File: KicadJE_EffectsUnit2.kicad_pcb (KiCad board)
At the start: 2 copper layers, 100 x 100 mm, 69 parts, among them J201 In_1, J202 In 2, J203 Out 1, J204 Out 2, J205 Out Final, P201 Doepfer_Power_10pin, SW201 Dist 6, SW202 In or cascade, SW203 In or cascade, SW204 In or cascade, SW205 HI/LO, U201 TL072, U202 TL072

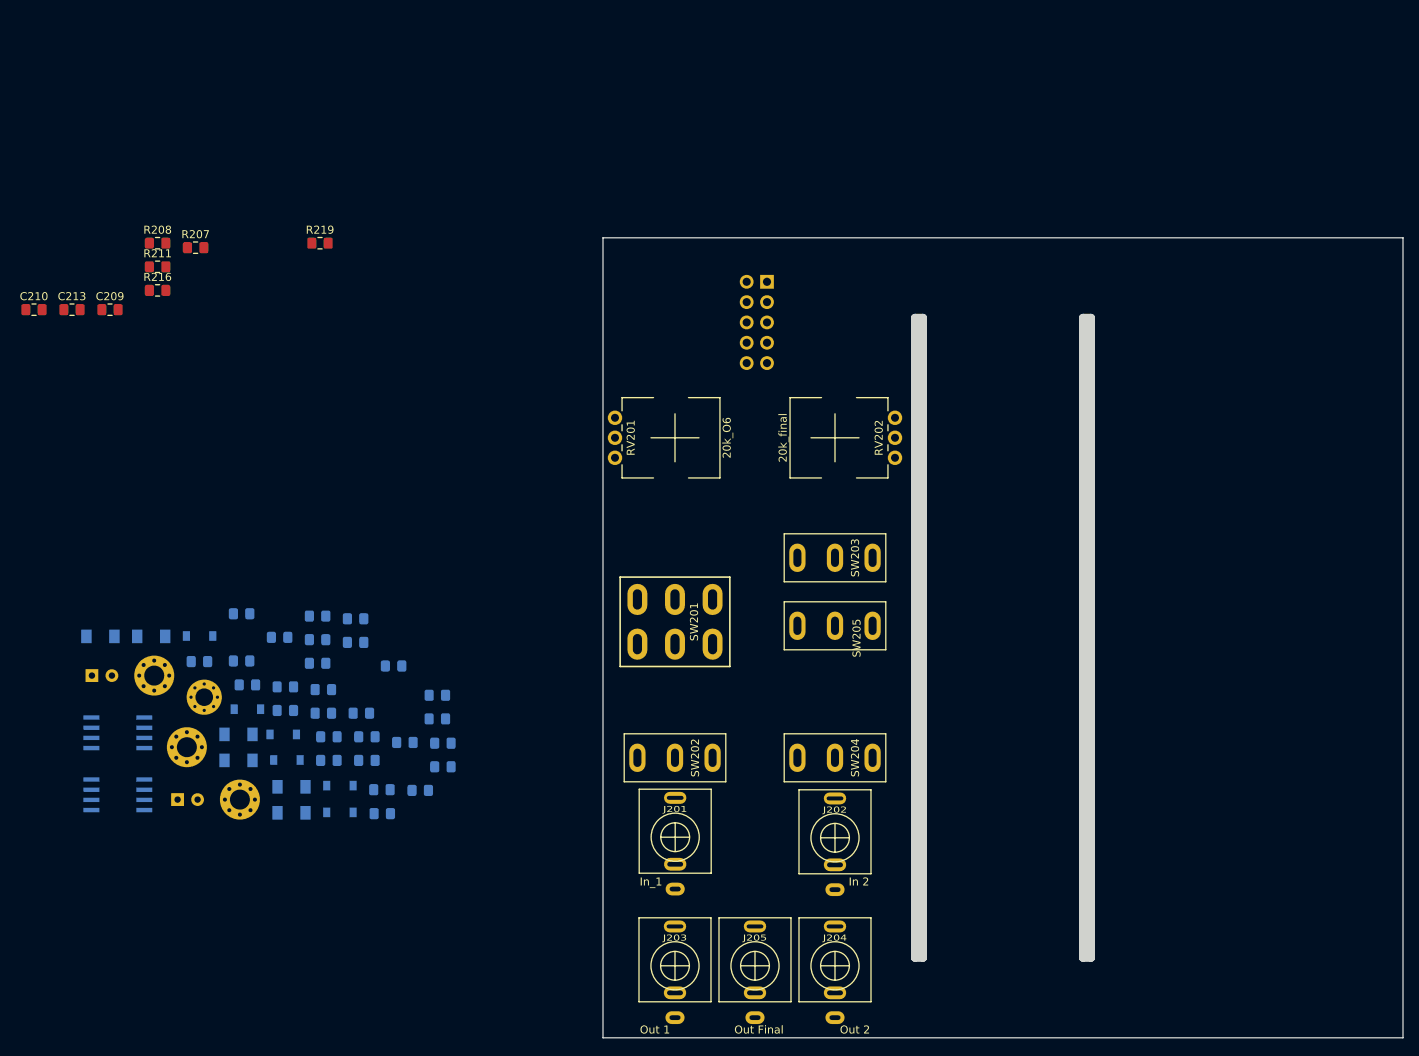
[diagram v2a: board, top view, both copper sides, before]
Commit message: decoupling placed
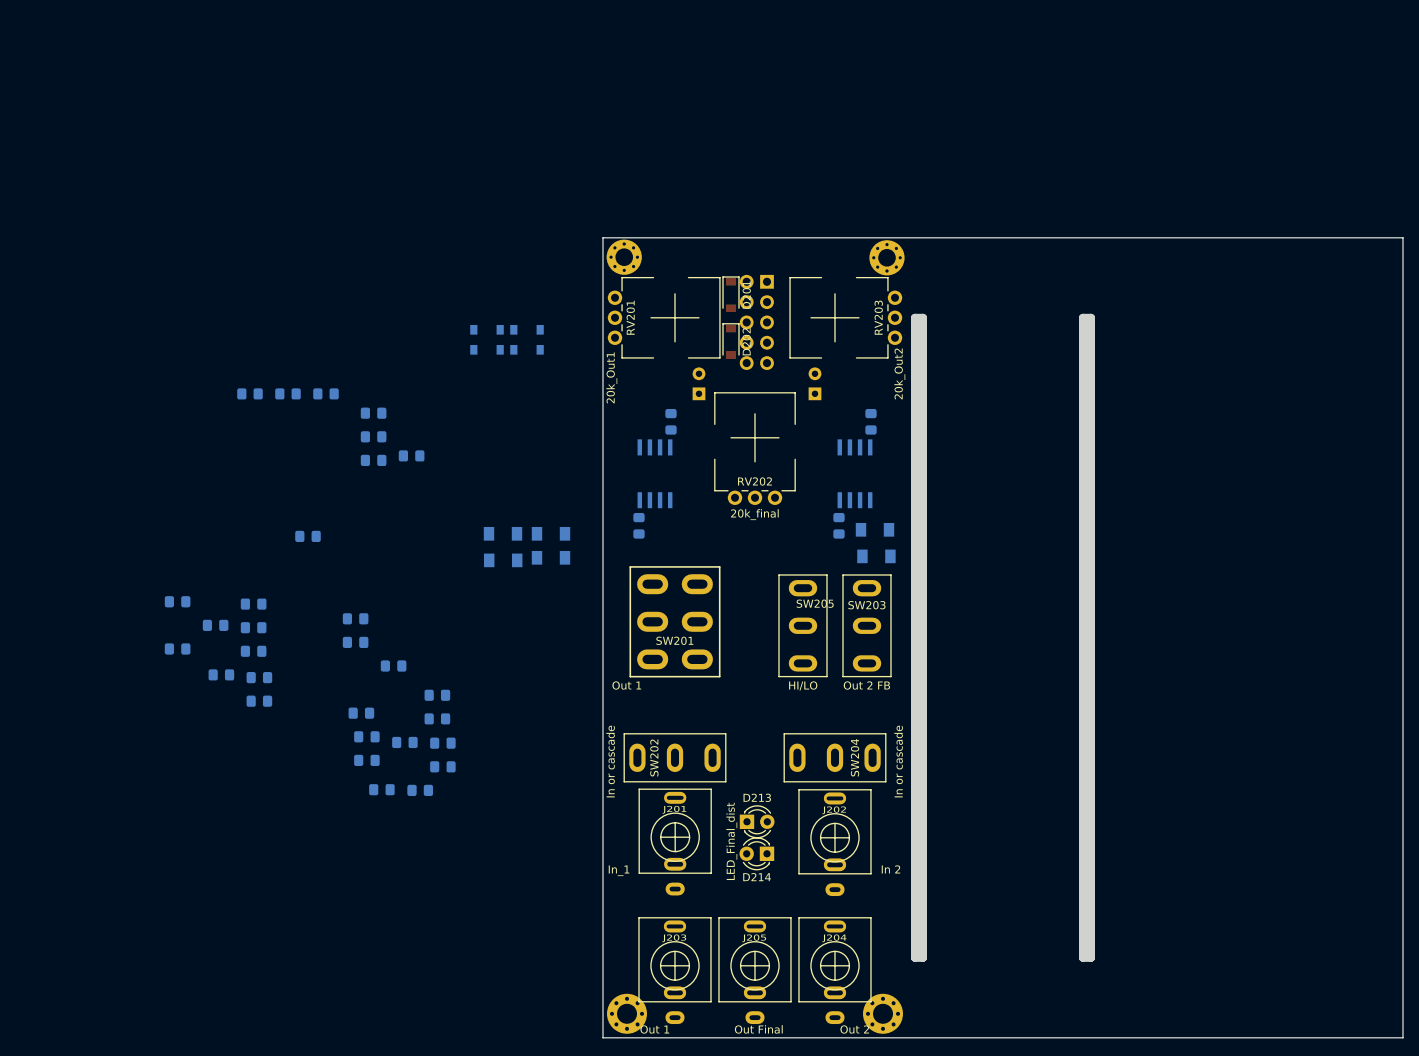
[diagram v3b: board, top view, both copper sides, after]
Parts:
- added RV203: 20k_Out2, Potentiometer_THT:Potentiometer_China_RK09_Single_Vertical_AJ, F.Cu at (86.5, 57.5)
- C209, C210, C213: value 100n -> 220n; moved to B.Cu
- C211: value 100n -> 220n
- D201, D202: moved to F.Cu
- D213: value LED_11dist -> LED_Final_dist; footprint LED_SMD:LED_0805_2012Metric_Pad1.15x1.40mm_HandSolder -> LED_THT:LED_D3.0mm; moved to F.Cu
- D214: value LED_11dist -> LED_Final_dist; footprint Diode_SMD:D_0805_2012Metric_Pad1.15x1.40mm_HandSolder -> LED_THT:LED_D3.0mm; moved to F.Cu
- H203: footprint MountingHole:MountingHole_2.5mm_Pad_Via -> MountingHole:MountingHole_2.2mm_M2_Pad_Via
- R206, R213: value 10k -> 4k7
- R207, R208, R211, R216, R219: moved to B.Cu
- RV201: value 20k_O6 -> 20k_Out1
- SW201: value Dist 6 -> Out 1
- SW203: value In or cascade -> Out 2 FB
- moved H203 105.4 mm to (85.5, 52.5)
- moved U202 100.5 mm to (81.5, 79.5), turned to 90 degrees
- moved D212 97.5 mm to (84.2, 89.8)
- moved C205 94.5 mm to (76.5, 69.5), turned to 90 degrees
- moved H202 93.2 mm to (85.0, 147.0)
- moved C203 89.1 mm to (83.5, 73.0), turned to 270 degrees
- moved D211 84.6 mm to (84.0, 86.5), turned to 180 degrees
- moved C201 83.7 mm to (62.0, 69.5), turned to 90 degrees
- moved D201 80.4 mm to (66.0, 57.1), turned to 270 degrees
- moved D202 76.5 mm to (66.0, 63.0), turned to 270 degrees
- moved H204 76.0 mm to (52.7, 52.4)
- moved U201 74.5 mm to (56.5, 79.5), turned to 90 degrees
- moved C207 73.0 mm to (79.5, 86.0), turned to 270 degrees
- moved D213 64.8 mm to (68.0, 123.0)
- moved D204 59.3 mm to (40.5, 64.0)
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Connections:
- C201 pad 1: (no net) -> /KicadJE_EU7_Distort2/-12v
- C201 pad 2: Net-(C201-Pad2) -> GND
- C202 pad 1: Net-(C202-Pad1) -> GND
- C202 pad 2: (no net) -> /KicadJE_EU7_Distort2/-12v
- C203 pad 1: Net-(C203-Pad1) -> GND
- C203 pad 2: (no net) -> /KicadJE_EU7_Distort2/-12v
- C205 pad 1: Net-(C201-Pad2) -> GND
- C205 pad 2: (no net) -> /KicadJE_EU7_Distort2/+12v
- C206 pad 1: (no net) -> /KicadJE_EU7_Distort2/+12v
- C206 pad 2: Net-(C202-Pad1) -> GND
- C207 pad 1: (no net) -> /KicadJE_EU7_Distort2/+12v
- C207 pad 2: Net-(C203-Pad1) -> GND
- C211 pad 2: (no net) -> Net-(C211-Pad2)
- D201 pad 1: (no net) -> /KicadJE_EU7_Distort2/-12v
- D201 pad 2: Net-(D201-Pad2) -> GND
- D202 pad 1: Net-(D201-Pad2) -> GND
- D202 pad 2: (no net) -> /KicadJE_EU7_Distort2/+12v
- D213 pad 2: OutFinal -> Net-(D213-Pad2)
- D214 pad 1: OutFinal -> Net-(D213-Pad2)
- P201 pad 1: +12V -> /KicadJE_EU7_Distort2/-12v
- P201 pad 10: -12V -> /KicadJE_EU7_Distort2/+12v
- P201 pad 2: +12V -> /KicadJE_EU7_Distort2/-12v
- P201 pad 3: Net-(P201-Pad3) -> GND
- P201 pad 4: Net-(P201-Pad3) -> GND
- P201 pad 5: Net-(P201-Pad3) -> GND
- P201 pad 6: Net-(P201-Pad3) -> GND
- P201 pad 7: Net-(P201-Pad3) -> GND
- P201 pad 8: Net-(P201-Pad3) -> GND
- P201 pad 9: -12V -> /KicadJE_EU7_Distort2/+12v
- R208 pad 2: (no net) -> In1
- R213 pad 2: Net-(R212-Pad1) -> Net-(R213-Pad2)
- R220 pad 1: OutFinal -> Net-(D213-Pad2)
- SW201 pad 2: (no net) -> Net-(D203-Pad2)
- SW203 pad 3: (no net) -> Net-(C211-Pad2)
- U201 pad 4: (no net) -> /KicadJE_EU7_Distort2/+12v
- U201 pad 8: (no net) -> /KicadJE_EU7_Distort2/-12v
- U202 pad 4: (no net) -> /KicadJE_EU7_Distort2/+12v
- U202 pad 5: (no net) -> Net-(D213-Pad2)
- U202 pad 6: (no net) -> OutFinal
- U202 pad 7: (no net) -> OutFinal
- U202 pad 8: (no net) -> /KicadJE_EU7_Distort2/-12v

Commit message: Overall placement
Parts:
- moved C211 101.6 mm to (97.0, 68.0)
- moved R214 99.3 mm to (97.0, 71.0)
- moved R213 98.5 mm to (97.0, 65.0)
- moved R222 90.5 mm to (92.5, 68.0)
- moved R201 85.6 mm to (79.0, 125.5), turned to 90 degrees
- moved C213 85.4 mm to (95.0, 83.0), turned to 180 degrees
- moved R211 76.0 mm to (94.5, 95.5)
- moved R216 73.9 mm to (93.3, 88.4)
- moved R217 72.5 mm to (93.0, 112.8)
- moved R212 70.5 mm to (97.5, 114.5), turned to 180 degrees
- moved R218 69.4 mm to (94.5, 108.5)
- moved C212 65.7 mm to (80.0, 87.5), turned to 270 degrees
- moved R215 65.5 mm to (80.0, 83.5), turned to 90 degrees
- moved C210 54.1 mm to (56.1, 89.5), turned to 180 degrees
- moved R202 50.2 mm to (76.0, 125.5), turned to 270 degrees
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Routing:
- net /KicadJE_EU7_Distort2/-12v: track 0.00 -> 72.4 mm
- net /KicadJE_EU7_Distort2/+12v: track 0.00 -> 71.7 mm
- net Net-(R212-Pad1): track 0.00 -> 38.0 mm
- net GND: track 0.00 -> 4.55 mm
- net Out1Dist: track 0.00 -> 2.50 mm
- net Net-(R220-Pad2): track 0.00 -> 2.50 mm

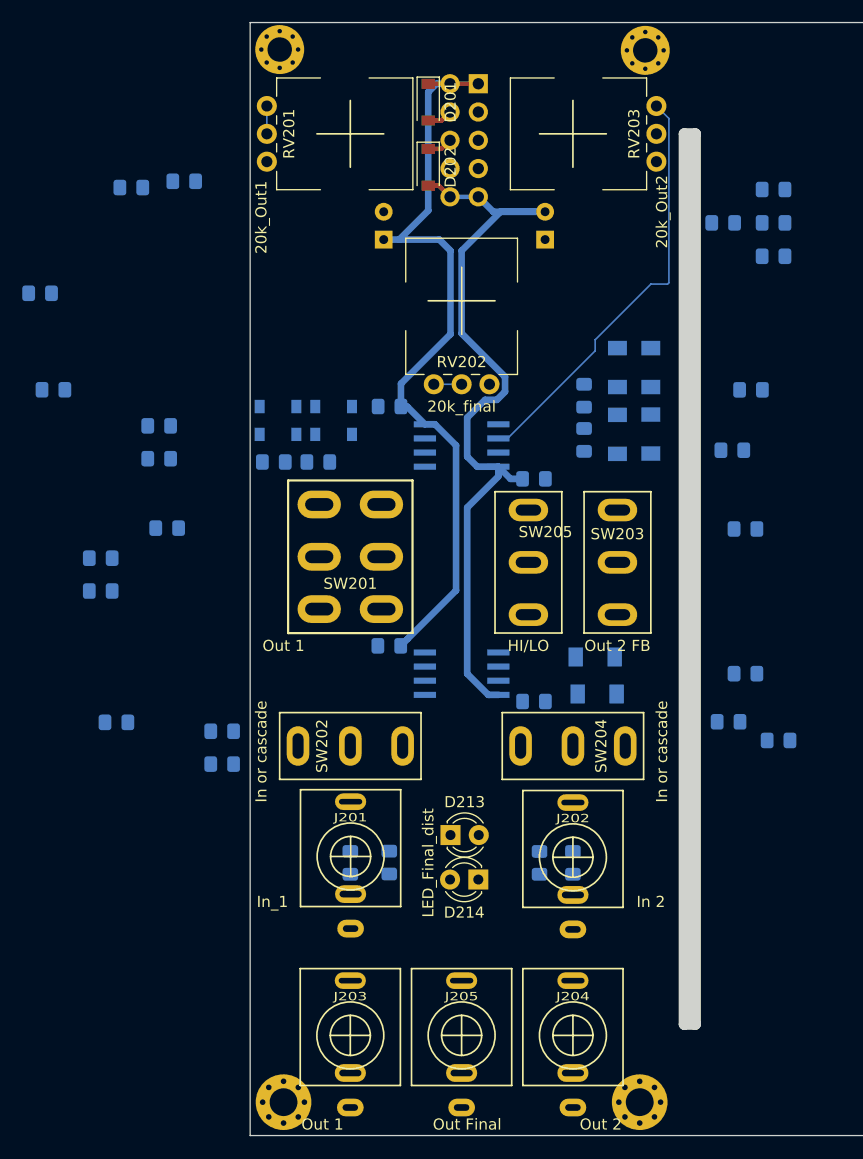
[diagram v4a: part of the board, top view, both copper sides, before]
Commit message: overall design places and routed
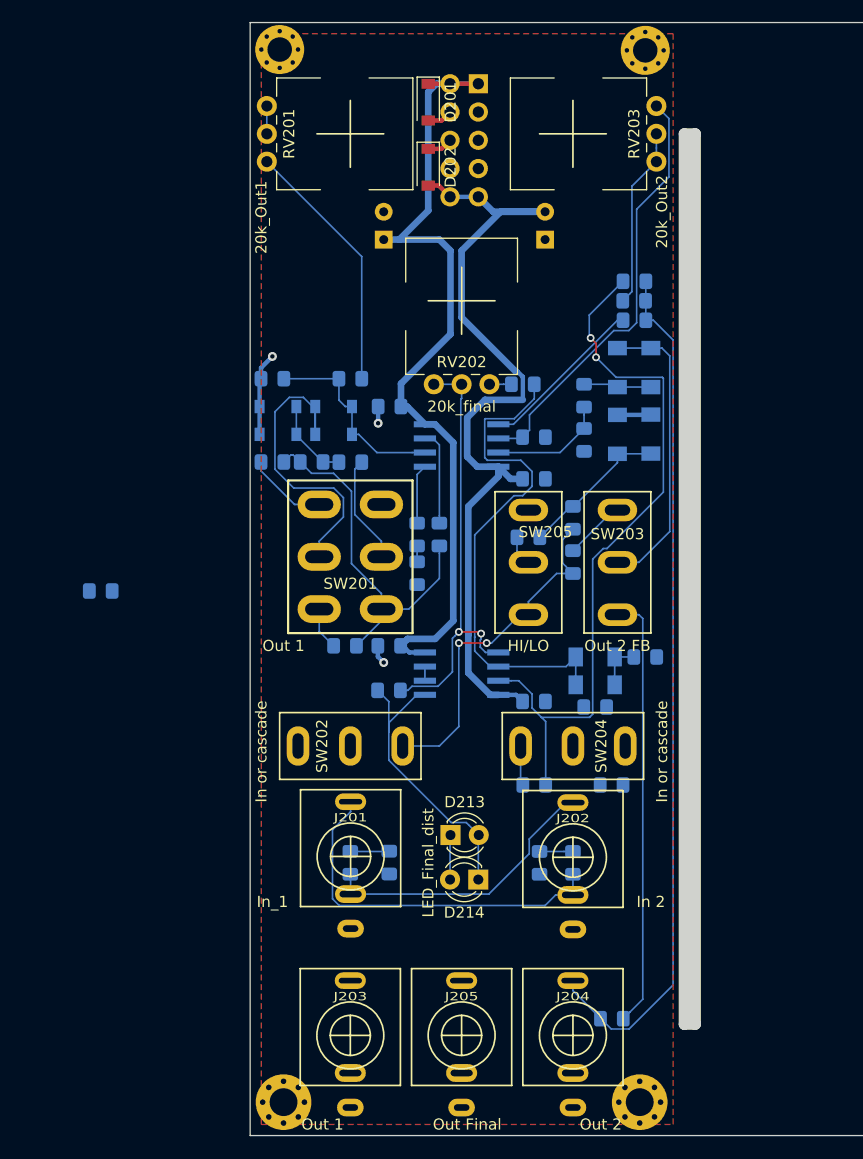
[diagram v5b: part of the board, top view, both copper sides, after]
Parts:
- moved C211 73.0 mm to (82.5, 139.5)
- moved R219 63.4 mm to (85.5, 107.0)
- moved C208 50.2 mm to (82.5, 118.5)
- moved R207 44.2 mm to (58.5, 106.0), turned to 180 degrees
- moved R208 40.4 mm to (65.0, 96.0), turned to 270 degrees
- moved R212 35.0 mm to (75.5, 87.2), turned to 0 degrees
- moved R209 33.6 mm to (67.0, 96.0), turned to 90 degrees
- moved R218 32.8 mm to (74.5, 82.5)
- moved R221 28.5 mm to (75.5, 118.5), turned to 180 degrees
- moved R210 27.5 mm to (59.0, 89.5), turned to 180 degrees
- moved C213 24.0 mm to (75.0, 96.2), turned to 0 degrees
- moved C204 22.8 mm to (65.0, 99.5), turned to 90 degrees
- moved R206 17.7 mm to (59.0, 82.0), turned to 180 degrees
- moved R220 16.4 mm to (62.5, 110.0)
- moved R213 16.0 mm to (84.5, 75.0), turned to 180 degrees
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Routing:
- net Out2Dist: track 0.00 -> 109.1 mm, vias 0 -> 2
- net Net-(R221-Pad1): track 0.00 -> 65.1 mm, vias 0 -> 2
- net Net-(D211-Pad2): track 0.00 -> 46.0 mm
- net Net-(C211-Pad2): track 0.00 -> 39.1 mm
- net Net-(R220-Pad2): track 2.50 -> 39.2 mm, vias 0 -> 2
- net Out1Dist: track 2.50 -> 39.0 mm
- net Net-(J201-PadT): track 0.00 -> 33.5 mm
- net Net-(D203-Pad2): track 0.00 -> 27.9 mm
- net Net-(D213-Pad2): track 0.00 -> 27.5 mm
- net Net-(D207-Pad2): track 0.00 -> 26.6 mm
- net Net-(J201-PadTN): track 0.00 -> 25.9 mm
- net Net-(R206-Pad1): track 0.00 -> 23.0 mm
- net Net-(D203-Pad1): track 0.00 -> 18.0 mm
- net Net-(R213-Pad2): track 0.00 -> 16.3 mm
- net Net-(R214-Pad2): track 0.00 -> 15.1 mm
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- added copper zone on F.Cu, net GND

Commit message: Routed
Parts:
- moved R223 33.0 mm to (62.5, 121.5), turned to 90 degrees
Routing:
- net Out1Dist: track 39.0 -> 160.7 mm
- net OutFinal: track 1.27 -> 49.1 mm, vias 0 -> 2
- net Net-(D207-Pad1): track 6.10 -> 50.3 mm, vias 0 -> 2
- net Net-(C204-Pad1): track 3.00 -> 38.1 mm, vias 0 -> 6
- net Net-(C208-Pad1): track 3.51 -> 32.4 mm
- net Out2Dist: track 109.1 -> 137.6 mm, vias 2 -> 4
- net Net-(R208-Pad1): track 5.36 -> 30.9 mm, vias 0 -> 2
- net In1: track 1.42 -> 24.4 mm, vias 0 -> 2
- net GND: track 18.3 -> 38.5 mm, vias 3 -> 11
- net Net-(D213-Pad1): track 4.02 -> 9.70 mm
- net In2: track 0.00 -> 3.58 mm
- net Net-(J201-PadTN): track 25.9 -> 29.1 mm
- net Net-(D211-Pad2): track 46.0 -> 48.3 mm
- net Net-(D207-Pad2): track 26.6 -> 25.6 mm
- net Net-(J201-PadT): track 33.5 -> 34.5 mm
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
